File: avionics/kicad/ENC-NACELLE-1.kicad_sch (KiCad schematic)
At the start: 4 parts, among them P1 PIGTAIL_7W, U1 AK7455

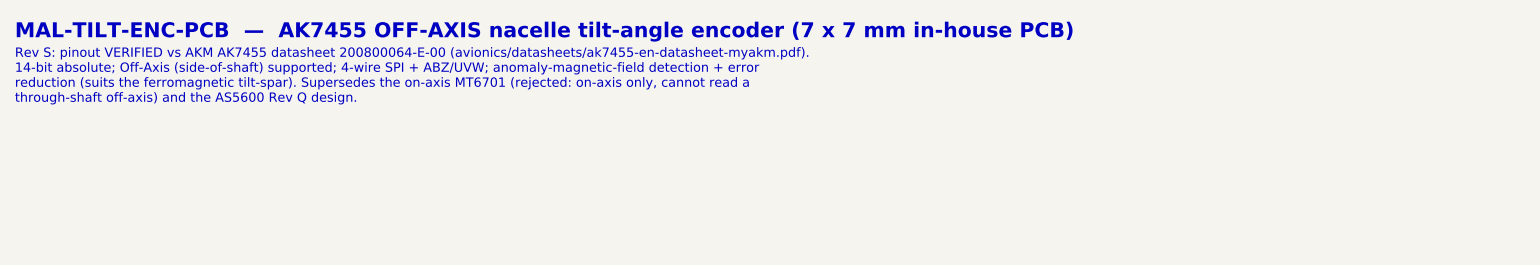
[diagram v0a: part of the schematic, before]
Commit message: Rename avionics/GCS boards off Firefly character names (TODO.md §0.9 item 8)
User-directed rename to close out the last open item from the licensing audit:
Malcolm/Mal -> Skipper, Wash -> Pilot, Zoe -> XO, Kaylee -> Flight Engineer,
Emma -> Commo, Jayne -> Observer. The four avionics bay names (Shepherd's Room,
Inara's Shuttle, River's Room, Simon's Medbay) were not part of this rename.

- Physical rename of all 198 board-folder paths via git mv: KiCad schematics,
  PCBs, gerbers, scripts, companion docs, plus the 6 shared Jayne_*.kicad_sym
  symbol libraries (authored under Jayne, reused fleet-wide by Wash/Kaylee/Emma/
  CAN-PERIPH-GW-1) -> Observer_*.kicad_sym, with every sym-lib-table/
  fp-lib-table/embedded lib_symbols reference updated to match. Also caught a
  second gerber export set outside the per-board folders and 4 STL BOM
  placeholders.
- Content sweep of ~5,800 substitutions across ~330 tracked text files, using
  word-boundary regex for the safe general case plus a small set of
  hand-verified literal-substring rules for snake_case identifiers. Verified
  before running that a blanket "mal_"/"emma" substring replace would have
  corrupted real unrelated tokens already in the repo (Blender normal_z
  surface-normal variables, KiCad thermal_pads/thermal_gap/thermal_bridge_width
  settings, "washer", "piezoelectric") -- used explicit rules instead and
  confirmed all four survived intact.
- MAL-* BOM/component designators renamed to SKIPPER-* consistently, including
  inside ENC-NACELLE-1 and CAN-PERIPH-GW-1's own netlists (cross-board net
  names).
- AGENTS.md Sec 9 naming table rewritten: dropped the Firefly-quote column from
  the live table (a mutated quote next to the new name would still signal the
  original character) and added a "Naming history" subsection recording the
  former names/inspirations/quotes for attribution completeness.
- Not verified: KiCad ERC/DRC -- no kicad-cli in this build environment. Every
  renamed symbol/lib-id/net strin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
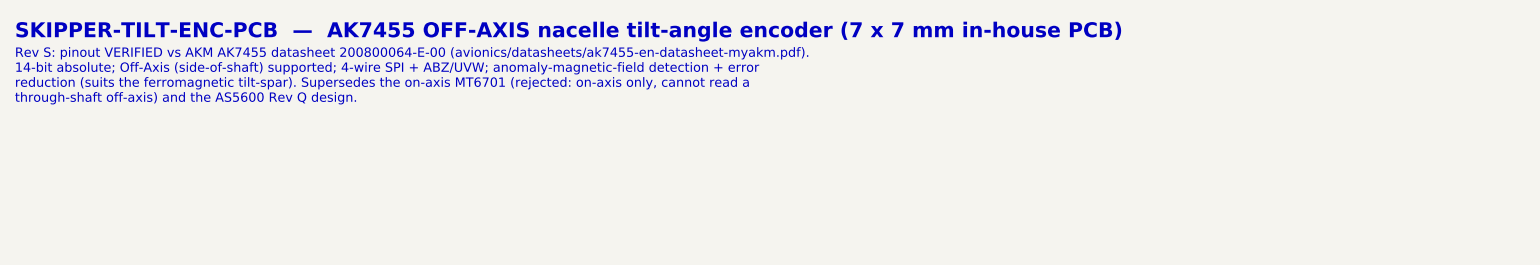
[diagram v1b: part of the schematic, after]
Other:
- note added: "SKIPPER-TILT-ENC-PCB — AK7455 OFF-AXIS nacelle tilt-angle encoder (7 x 7 mm in-house PCB)"
- note removed: "MAL-TILT-ENC-PCB — AK7455 OFF-AXIS nacelle tilt-angle encoder (7 x 7 mm in-house PCB)"
- title: ENC-NACELLE-1 / MAL-TILT-ENC-PCB — Nacelle Tilt-Angle Encoder (AK7455, off-axis) -> ENC-NACELLE-1 / SKIPPER-TILT-ENC-PCB — Nacelle Tilt-Angle Encoder (AK7455, off-axis)
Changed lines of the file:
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@@
   (paper "A4")
   (title_block
-    (title "ENC-NACELLE-1 / MAL-TILT-ENC-PCB — Nacelle Tilt-Angle Encoder (AK7455, off-axis)")
+    (title "ENC-NACELLE-1 / SKIPPER-TILT-ENC-PCB — Nacelle Tilt-Angle Encoder (AK7455, off-axis)")
     (date "2026-07-19")
     (rev "S")
@@
     (comment 4 "SPI (not I2C): both nacelles share the bus via separate CSN. TEST2->VSS, TEST1 open, NC pins + back-tab OPEN")
   )
-  (text "MAL-TILT-ENC-PCB  —  AK7455 OFF-AXIS nacelle tilt-angle encoder (7 x 7 mm in-house PCB)"
+  (text "SKIPPER-TILT-ENC-PCB  —  AK7455 OFF-AXIS nacelle tilt-angle encoder (7 x 7 mm in-house PCB)"
     (at 24.00 22.00 0)
     (effects (font (size 2.0 2.0) (bold yes)) (justify left))
